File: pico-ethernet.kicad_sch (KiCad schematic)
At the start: 28 parts, among them J1 Conn_01x20_Pin, J2 Conn_01x02_Pin, J3 VR05S05, J4 SI-52003-F, J5 Conn_01x02, U1 ENC28J60x-SS, Y1 25MHz

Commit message: interrupt
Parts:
- J2: footprint Connector_PinSocket_2.54mm:PinSocket_1x04_P2.54mm_Vertical -> Connector_PinSocket_2.54mm:PinSocket_1x05_P2.54mm_Vertical; symbol Connector:Conn_01x04_Pin -> Connector:Conn_01x05_Pin
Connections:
- net at U1.4 (~{INT}): now also J2.5 (Pin_5)
- no-connect marks 17 -> 16
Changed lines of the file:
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@@
 	)
 	(no_connect
-		(at 105.41 83.82)
-	)
-	(no_connect
 		(at 82.55 48.26)
 	)
@@
 	(wire
 		(pts
-			(xy 46.99 57.15) (xy 46.99 54.61)
+			(xy 46.99 52.07) (xy 46.99 57.15)
+		)
+		(stroke
+			(width 0)
+			(type default)
+		)
+	)
+	(wire
+		(pts
+			(xy 72.39 64.77) (xy 36.83 64.77)
 		)
 		(stroke
@@
 	(wire
 		(pts
-			(xy 36.83 59.69) (xy 40.64 59.69)
+			(xy 52.07 54.61) (xy 52.07 62.23)
 		)
 		(stroke
@@
 	(wire
 		(pts
-			(xy 52.07 54.61) (xy 52.07 62.23)
+			(xy 166.37 77.47) (xy 166.37 80.01)
 		)
 		(stroke
@@
 	(wire
 		(pts
-			(xy 166.37 77.47) (xy 166.37 80.01)
+			(xy 151.13 101.6) (xy 152.4 101.6)
 		)
 		(stroke
@@
 	(wire
 		(pts
-			(xy 151.13 101.6) (xy 152.4 101.6)
+			(xy 82.55 81.28) (xy 97.79 81.28)
 		)
 		(stroke
@@
 	(wire
 		(pts
-			(xy 82.55 81.28) (xy 97.79 81.28)
+			(xy 46.99 52.07) (xy 36.83 52.07)
 		)
 		(stroke
@@
 	(wire
 		(pts
-			(xy 125.73 52.07) (xy 113.03 52.07)
+			(xy 40.64 57.15) (xy 36.83 57.15)
 		)
 		(stroke
@@
 	(wire
 		(pts
-			(xy 176.53 99.06) (xy 160.02 99.06)
+			(xy 125.73 52.07) (xy 113.03 52.07)
 		)
 		(stroke
@@
 	(wire
 		(pts
-			(xy 100.33 99.06) (xy 100.33 100.33)
+			(xy 176.53 99.06) (xy 160.02 99.06)
 		)
 		(stroke
@@
 	(wire
 		(pts
-			(xy 166.37 80.01) (xy 166.37 82.55)
+			(xy 100.33 99.06) (xy 100.33 100.33)
 		)
 		(stroke
@@
 	(wire
 		(pts
-			(xy 229.87 97.79) (xy 229.87 102.87)
+			(xy 166.37 80.01) (xy 166.37 82.55)
 		)
 		(stroke
@@
 	(wire
 		(pts
-			(xy 36.83 54.61) (xy 46.99 54.61)
+			(xy 229.87 97.79) (xy 229.87 102.87)
 		)
 		(stroke
@@
 	(wire
 		(pts
+			(xy 105.41 82.55) (xy 72.39 82.55)
+		)
+		(stroke
+			(width 0)
+			(type default)
+		)
+	)
+	(wire
+		(pts
 			(xy 105.41 73.66) (xy 97.79 73.66)
 		)
@@
 	(wire
 		(pts
-			(xy 36.83 52.07) (xy 43.18 52.07)
-		)
-		(stroke
-			(width 0)
-			(type default)
-		)
-	)
-	(wire
-		(pts
 			(xy 132.08 54.61) (xy 142.24 54.61)
 		)
@@
 	(wire
 		(pts
-			(xy 40.64 62.23) (xy 40.64 59.69)
+			(xy 40.64 57.15) (xy 40.64 62.23)
 		)
 		(stroke
@@
 	(wire
 		(pts
-			(xy 43.18 52.07) (xy 43.18 59.69)
+			(xy 43.18 49.53) (xy 43.18 59.69)
 		)
 		(stroke
@@
 	(wire
 		(pts
+			(xy 72.39 82.55) (xy 72.39 64.77)
+		)
+		(stroke
+			(width 0)
+			(type default)
+		)
+	)
+	(wire
+		(pts
 			(xy 120.65 153.67) (xy 120.65 143.51)
 		)
@@
 	(wire
 		(pts
+			(xy 43.18 49.53) (xy 36.83 49.53)
+		)
+		(stroke
+			(width 0)
+			(type default)
+		)
+	)
+	(wire
+		(pts
 			(xy 209.55 95.25) (xy 232.41 95.25)
 		)
@@
 	(wire
 		(pts
+			(xy 36.83 64.77) (xy 36.83 59.69)
+		)
+		(stroke
+			(width 0)
+			(type default)
+		)
+	)
+	(wire
+		(pts
 			(xy 82.55 78.74) (xy 105.41 78.74)
 		)
@@
 	(wire
 		(pts
+			(xy 105.41 83.82) (xy 105.41 82.55)
+		)
+		(stroke
+			(width 0)
+			(type default)
+		)
+	)
+	(wire
+		(pts
 			(xy 73.66 100.33) (xy 78.74 100.33)
 		)
@@
 			)
 		)
-		(property "Datasheet" ""
+		(property "Datasheet" "https://www.belfuse.com/resources/drawings/magneticsolutions/dr-mag-si-52003-f.pdf"
 			(at 245.11 87.63 0)
 			(effects
@@
 		(lib_name "GND_1")
 		(lib_id "power:GND")
-		(at 36.83 57.15 90)
+		(at 36.83 54.61 90)
 		(unit 1)
 		(exclude_from_sim no)
@@
 		(dnp no)
 		(property "Reference" "#PWR021"
-			(at 43.18 57.15 0)
+			(at 43.18 54.61 0)
 			(effects
 				(font
@@
 		)
 		(property "Value" "GND"
-			(at 40.132 57.15 90)
+			(at 40.132 54.61 90)
 			(effects
 				(font
@@
 		)
 		(property "Footprint" ""
-			(at 36.83 57.15 0)
+			(at 36.83 54.61 0)
 			(effects
 				(font
@@
 		)
 		(property "Datasheet" ""
-			(at 36.83 57.15 0)
+			(at 36.83 54.61 0)
 			(effects
 				(font
@@
 		)
 		(property "Description" "Power symbol creates a global label with name \"GND\" , ground"
-			(at 36.83 57.15 0)
+			(at 36.83 54.61 0)
 			(effects
 				(font
@@
 			)
 		)
-		(property "Datasheet" "VR05S05"
+		(property "Datasheet" "https://www.xppower.com/portals/0/pdfs/SF_VR05.pdf"
 			(at 102.87 156.21 0)
 			(effects
@@
 	)
 	(symbol
-		(lib_id "Connector:Conn_01x04_Pin")
+		(lib_id "Connector:Conn_01x05_Pin")
 		(at 31.75 54.61 0)
 		(unit 1)
@@
 		(fields_autoplaced yes)
 		(property "Reference" "J2"
-			(at 32.385 46.99 0)
+			(at 32.385 44.45 0)
 			(effects
 				(font
@@
 		)
 		(property "Value" "Conn_01x02_Pin"
-			(at 32.385 49.53 0)
+			(at 32.385 46.99 0)
 			(effects
 				(font
@@
 			)
 		)
-		(property "Footprint" "Connector_PinSocket_2.54mm:PinSocket_1x04_P2.54mm_Vertical"
+		(property "Footprint" "Connector_PinSocket_2.54mm:PinSocket_1x05_P2.54mm_Vertical"
 			(at 31.75 54.61 0)
 			(effects
@@
 			)
 		)
-		(property "Description" "Generic connector, single row, 01x04, script generated"
+		(property "Description" "Generic connector, single row, 01x05, script generated"
 			(at 31.75 54.61 0)
 			(effects
@@
 		(pin "4"
 		)
+		(pin "5"
+		)
 		(instances
 			(project "pico-ethernet"
@@
 			)
 		)
-		(property "Datasheet" "http://ww1.microchip.com/downloads/en/devicedoc/39662e.pdf"
+		(property "Datasheet" "https://ww1.microchip.com/downloads/en/DeviceDoc/39662e.pdf"
 			(at 123.19 86.36 0)
 			(effects
@@
 			)
 		)
-		(property "Datasheet" "~"
+		(property "Datasheet" "https://media.digikey.com/pdf/Data%20Sheets/CTS%20Corporation%20PDFs/445_Series.pdf"
 			(at 92.71 96.52 0)
 			(effects

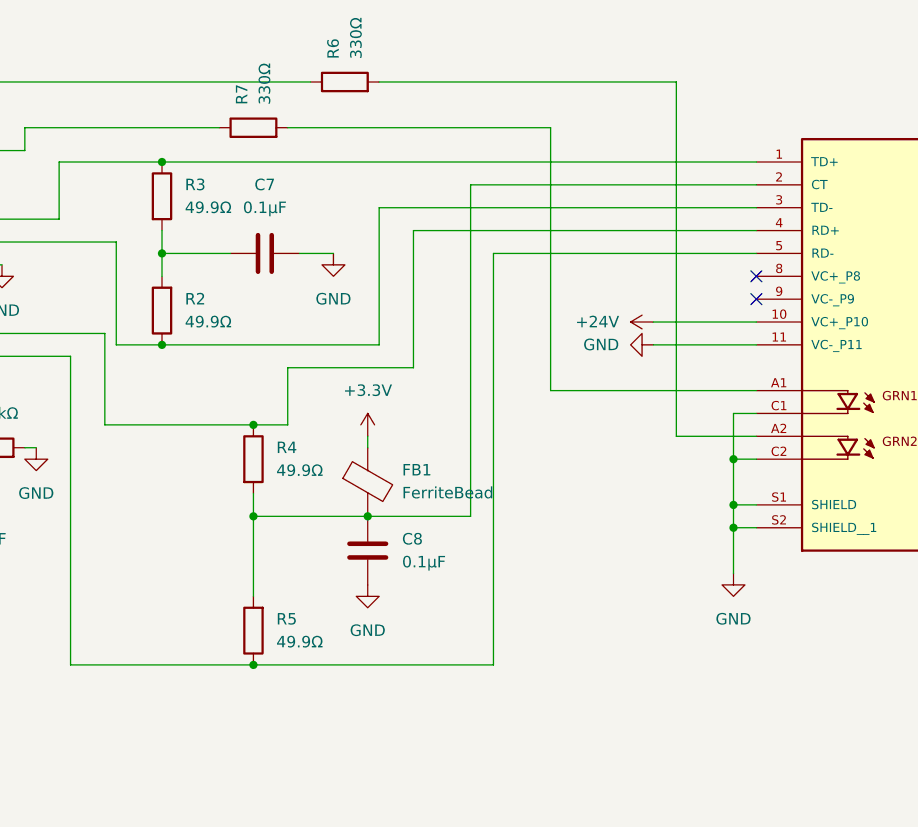
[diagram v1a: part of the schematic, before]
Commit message: TX RX swap
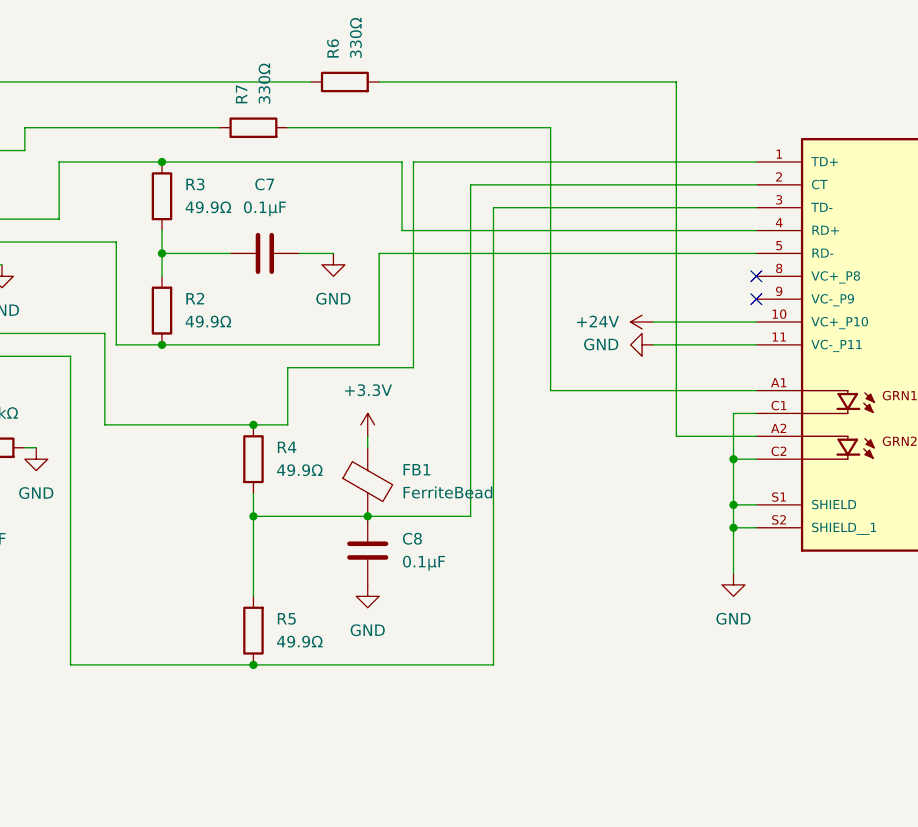
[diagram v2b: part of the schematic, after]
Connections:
- net at R3.1, U1.13 (TPIN+): now also J4.4 (RD+); no longer J4.1 (TD+)
- net at R2.1, U1.12 (TPIN-): now also J4.5 (RD-); no longer J4.3 (TD-)
- net at R4.1, U1.17 (TPOUT+): now also J4.1 (TD+); no longer J4.4 (RD+)
- net at R5.1, U1.16 (TPOUT-): now also J4.3 (TD-); no longer J4.5 (RD-)
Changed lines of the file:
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@@
+	)
+	(junction
+		(at 229.87 102.87)
+		(diameter 0)
+		(color 0 0 0 0)
+	)
+	(junction
+		(at 125.73 52.07)
+		(diameter 0)
+		(color 0 0 0 0)
+	)
+	(junction
+		(at 144.78 52.07)
+		(diameter 0)
+		(color 0 0 0 0)
+	)
+	(junction
+		(at 176.53 125.73)
+		(diameter 0)
+		(color 0 0 0 0)
+	)
+	(junction
+		(at 176.53 109.22)
+		(diameter 0)
+		(color 0 0 0 0)
+	)
+	(junction
+		(at 176.53 99.06)
+		(diameter 0)
+		(color 0 0 0 0)
+	)
+	(junction
+		(at 166.37 80.01)
+		(diameter 0)
+		(color 0 0 0 0)
+	)
+	(junction
+		(at 125.73 44.45)
+		(diameter 0)
+		(color 0 0 0 0)
+	)
+	(junction
+		(at 101.6 114.3)
+		(diameter 0)
+		(color 0 0 0 0)
+	)
+	(junction
+		(at 73.66 92.71)
+		(diameter 0)
+		(color 0 0 0 0)
+	)
+	(junction
+		(at 132.08 52.07)
+		(diameter 0)
+		(color 0 0 0 0)
+	)
+	(junction
+		(at 229.87 110.49)
+		(diameter 0)
+		(color 0 0 0 0)
+	)
+	(junction
+		(at 189.23 109.22)
+		(diameter 0)
+		(color 0 0 0 0)
+	)
+	(junction
+		(at 120.65 114.3)
+		(diameter 0)
+		(color 0 0 0 0)
+	)
+	(junction
+		(at 102.87 151.13)
+		(diameter 0)
+		(color 0 0 0 0)
+	)
+	(junction
+		(at 125.73 156.21)
+		(diameter 0)
+		(color 0 0 0 0)
 	)
 	(junction
@@
 	)
 	(junction
-		(at 229.87 102.87)
-		(diameter 0)
-		(color 0 0 0 0)
-	)
-	(junction
-		(at 125.73 52.07)
-		(diameter 0)
-		(color 0 0 0 0)
-	)
-	(junction
-		(at 144.78 52.07)
-		(diameter 0)
-		(color 0 0 0 0)
-	)
-	(junction
-		(at 176.53 125.73)
-		(diameter 0)
-		(color 0 0 0 0)
-	)
-	(junction
-		(at 176.53 109.22)
-		(diameter 0)
-		(color 0 0 0 0)
-	)
-	(junction
-		(at 176.53 99.06)
-		(diameter 0)
-		(color 0 0 0 0)
-	)
-	(junction
-		(at 166.37 80.01)
-		(diameter 0)
-		(color 0 0 0 0)
-	)
-	(junction
-		(at 125.73 44.45)
-		(diameter 0)
-		(color 0 0 0 0)
-	)
-	(junction
-		(at 101.6 114.3)
-		(diameter 0)
-		(color 0 0 0 0)
-	)
-	(junction
-		(at 73.66 92.71)
-		(diameter 0)
-		(color 0 0 0 0)
-	)
-	(junction
-		(at 132.08 52.07)
-		(diameter 0)
-		(color 0 0 0 0)
-	)
-	(junction
-		(at 229.87 110.49)
-		(diameter 0)
-		(color 0 0 0 0)
-	)
-	(junction
-		(at 189.23 109.22)
-		(diameter 0)
-		(color 0 0 0 0)
-	)
-	(junction
-		(at 120.65 114.3)
-		(diameter 0)
-		(color 0 0 0 0)
-	)
-	(junction
-		(at 102.87 151.13)
-		(diameter 0)
-		(color 0 0 0 0)
-	)
-	(junction
-		(at 125.73 156.21)
-		(diameter 0)
-		(color 0 0 0 0)
-	)
-	(junction
 		(at 132.08 44.45)
 		(diameter 0)
@@
 	(wire
 		(pts
+			(xy 203.2 74.93) (xy 232.41 74.93)
+		)
+		(stroke
+			(width 0)
+			(type default)
+		)
+	)
+	(wire
+		(pts
 			(xy 46.99 52.07) (xy 46.99 57.15)
 		)
@@
 	(wire
 		(pts
+			(xy 194.31 69.85) (xy 232.41 69.85)
+		)
+		(stroke
+			(width 0)
+			(type default)
+		)
+	)
+	(wire
+		(pts
+			(xy 203.2 74.93) (xy 203.2 125.73)
+		)
+		(stroke
+			(width 0)
+			(type default)
+		)
+	)
+	(wire
+		(pts
 			(xy 140.97 93.98) (xy 144.78 93.98)
 		)
@@
 	(wire
 		(pts
-			(xy 203.2 80.01) (xy 203.2 125.73)
-		)
-		(stroke
-			(width 0)
-			(type default)
-		)
-	)
-	(wire
-		(pts
 			(xy 52.07 54.61) (xy 52.07 62.23)
 		)
@@
 	(wire
 		(pts
-			(xy 194.31 77.47) (xy 194.31 92.71)
+			(xy 194.31 69.85) (xy 194.31 92.71)
 		)
 		(stroke
@@
 	(wire
 		(pts
-			(xy 232.41 74.93) (xy 190.5 74.93)
-		)
-		(stroke
-			(width 0)
-			(type default)
-		)
-	)
-	(wire
-		(pts
 			(xy 166.37 80.01) (xy 173.99 80.01)
 		)
@@
 	(wire
 		(pts
-			(xy 232.41 80.01) (xy 203.2 80.01)
-		)
-		(stroke
-			(width 0)
-			(type default)
-		)
-	)
-	(wire
-		(pts
 			(xy 132.08 52.07) (xy 144.78 52.07)
 		)
@@
 	(wire
 		(pts
+			(xy 190.5 80.01) (xy 232.41 80.01)
+		)
+		(stroke
+			(width 0)
+			(type default)
+		)
+	)
+	(wire
+		(pts
 			(xy 180.34 66.04) (xy 209.55 66.04)
 		)
@@
 	(wire
 		(pts
+			(xy 193.04 69.85) (xy 193.04 77.47)
+		)
+		(stroke
+			(width 0)
+			(type default)
+		)
+	)
+	(wire
+		(pts
 			(xy 232.41 107.95) (xy 229.87 107.95)
 		)
@@
 	(wire
 		(pts
-			(xy 166.37 69.85) (xy 232.41 69.85)
+			(xy 190.5 80.01) (xy 190.5 90.17)
 		)
 		(stroke
@@
 	(wire
 		(pts
-			(xy 232.41 77.47) (xy 194.31 77.47)
-		)
-		(stroke
-			(width 0)
-			(type default)
-		)
-	)
-	(wire
-		(pts
 			(xy 86.36 35.56) (xy 82.55 35.56)
 		)
@@
 	(wire
 		(pts
-			(xy 190.5 74.93) (xy 190.5 90.17)
-		)
-		(stroke
-			(width 0)
-			(type default)
-		)
-	)
-	(wire
-		(pts
 			(xy 189.23 109.22) (xy 200.66 109.22)
 		)
@@
 	(wire
 		(pts
+			(xy 166.37 69.85) (xy 193.04 69.85)
+		)
+		(stroke
+			(width 0)
+			(type default)
+		)
+	)
+	(wire
+		(pts
 			(xy 54.61 54.61) (xy 52.07 54.61)
 		)
@@
 		)
 		(stroke
+			(width 0)
+			(type default)
+		)
+	)
+	(wire
+		(pts
+			(xy 193.04 77.47) (xy 232.41 77.47)
+		)
+		(stroke

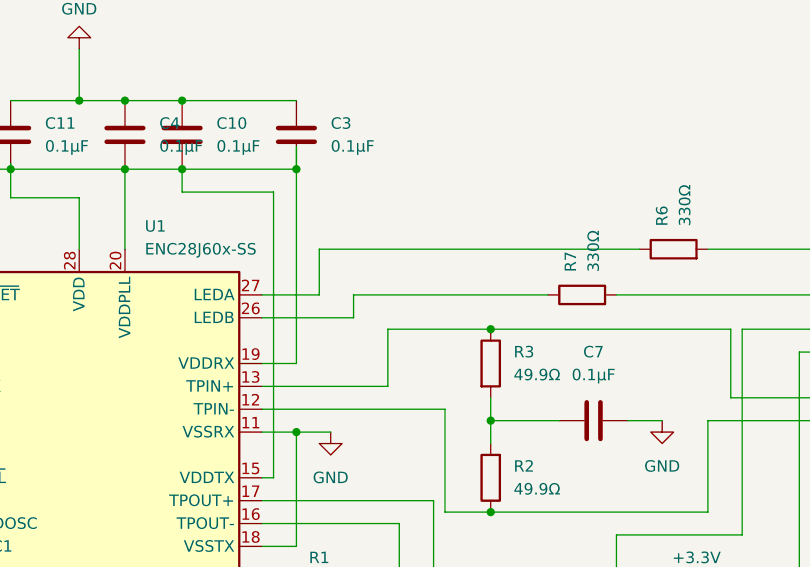
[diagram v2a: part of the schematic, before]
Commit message: 3v reroute
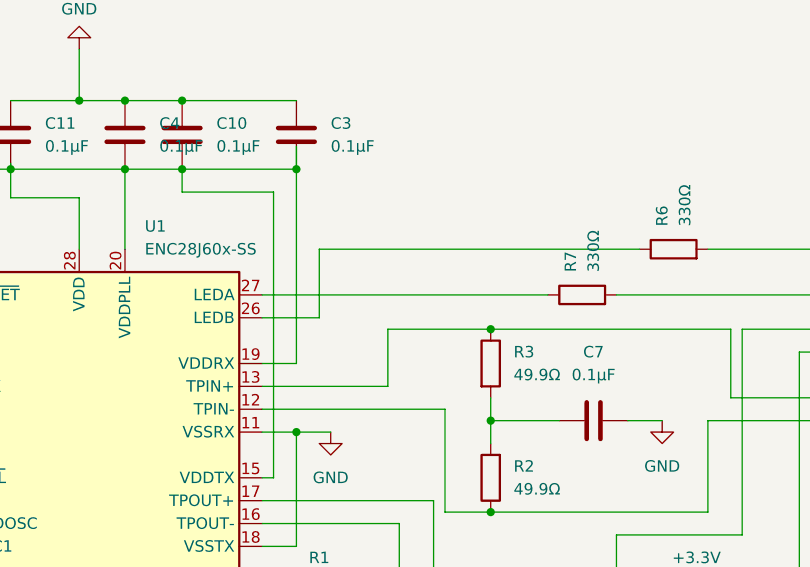
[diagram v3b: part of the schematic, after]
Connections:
- net at R6.1: now also U1.26 (LEDB); no longer U1.27 (LEDA)
- net at R7.1: now also U1.27 (LEDA); no longer U1.26 (LEDB)
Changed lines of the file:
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@@
-	(wire
-		(pts
-			(xy 151.13 68.58) (xy 140.97 68.58)
-		)
-		(stroke
-			(width 0)
-			(type default)
-		)
-	)
 	(wire
 		(pts
@@
 	(wire
 		(pts
-			(xy 140.97 66.04) (xy 147.32 66.04)
-		)
-		(stroke
-			(width 0)
-			(type default)
-		)
-	)
-	(wire
-		(pts
 			(xy 132.08 44.45) (xy 144.78 44.45)
 		)
@@
 	(wire
 		(pts
+			(xy 147.32 68.58) (xy 140.97 68.58)
+		)
+		(stroke
+			(width 0)
+			(type default)
+		)
+	)
+	(wire
+		(pts
 			(xy 181.61 80.01) (xy 185.42 80.01)
 		)
@@
 	(wire
 		(pts
-			(xy 172.72 66.04) (xy 151.13 66.04)
+			(xy 140.97 66.04) (xy 172.72 66.04)
 		)
 		(stroke
@@
 	(wire
 		(pts
-			(xy 147.32 60.96) (xy 147.32 66.04)
-		)
-		(stroke
-			(width 0)
-			(type default)
-		)
-	)
-	(wire
-		(pts
 			(xy 176.53 125.73) (xy 203.2 125.73)
 		)
@@
 	(wire
 		(pts
-			(xy 151.13 66.04) (xy 151.13 68.58)
-		)
-		(stroke
-			(width 0)
-			(type default)
-		)
-	)
-	(wire
-		(pts
 			(xy 144.78 81.28) (xy 148.59 81.28)
 		)
@@
 		)
 		(stroke
+			(width 0)
+			(type default)
+		)
+	)
+	(wire
+		(pts
+			(xy 147.32 60.96) (xy 147.32 68.58)
+		)
+		(stroke

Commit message: vanity
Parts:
- R6, R7: value 330Ω -> 180Ω
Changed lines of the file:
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@@
 	(wire
 		(pts
-			(xy 203.2 74.93) (xy 232.41 74.93)
+			(xy 205.74 74.93) (xy 232.41 74.93)
 		)
 		(stroke
@@
 	(wire
 		(pts
-			(xy 194.31 69.85) (xy 232.41 69.85)
+			(xy 196.85 69.85) (xy 232.41 69.85)
 		)
 		(stroke
@@
 	(wire
 		(pts
-			(xy 203.2 74.93) (xy 203.2 125.73)
+			(xy 205.74 74.93) (xy 205.74 125.73)
 		)
 		(stroke
@@
 	(wire
 		(pts
-			(xy 194.31 92.71) (xy 180.34 92.71)
+			(xy 196.85 92.71) (xy 180.34 92.71)
 		)
 		(stroke
@@
 	(wire
 		(pts
-			(xy 194.31 69.85) (xy 194.31 92.71)
+			(xy 196.85 69.85) (xy 196.85 92.71)
 		)
 		(stroke
@@
 	(wire
 		(pts
-			(xy 176.53 125.73) (xy 203.2 125.73)
+			(xy 176.53 125.73) (xy 205.74 125.73)
 		)
 		(stroke
@@
 	(wire
 		(pts
-			(xy 193.04 69.85) (xy 193.04 77.47)
+			(xy 190.5 69.85) (xy 190.5 77.47)
 		)
 		(stroke
@@
 	(wire
 		(pts
-			(xy 166.37 69.85) (xy 193.04 69.85)
+			(xy 166.37 69.85) (xy 190.5 69.85)
 		)
 		(stroke
@@
 	(wire
 		(pts
-			(xy 193.04 77.47) (xy 232.41 77.47)
+			(xy 190.5 77.47) (xy 232.41 77.47)
 		)
 		(stroke
@@
 			)
 		)
-		(property "Value" "330Ω"
+		(property "Value" "180Ω"
 			(at 187.96 58.42 0)
 			(effects
@@
 			)
 		)
-		(property "Value" "330Ω"
+		(property "Value" "180Ω"
 			(at 177.8 63.5 0)
 			(effects

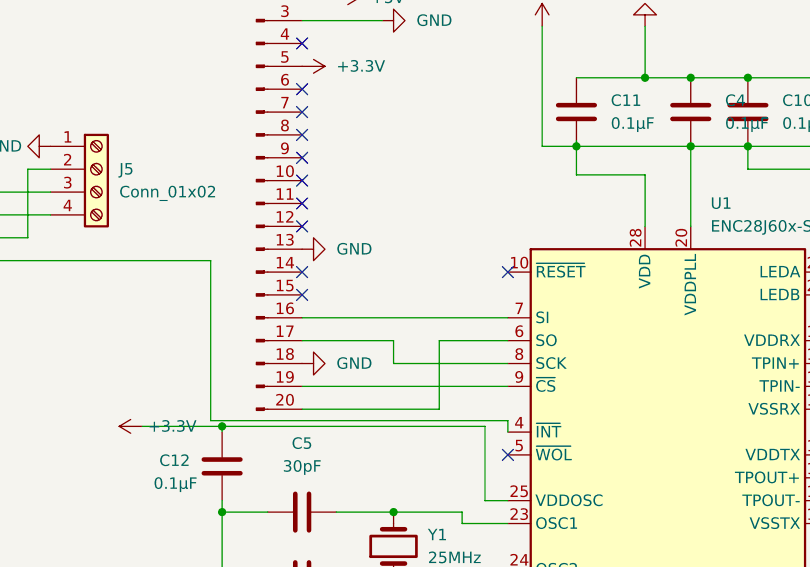
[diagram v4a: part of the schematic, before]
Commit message: connect reset
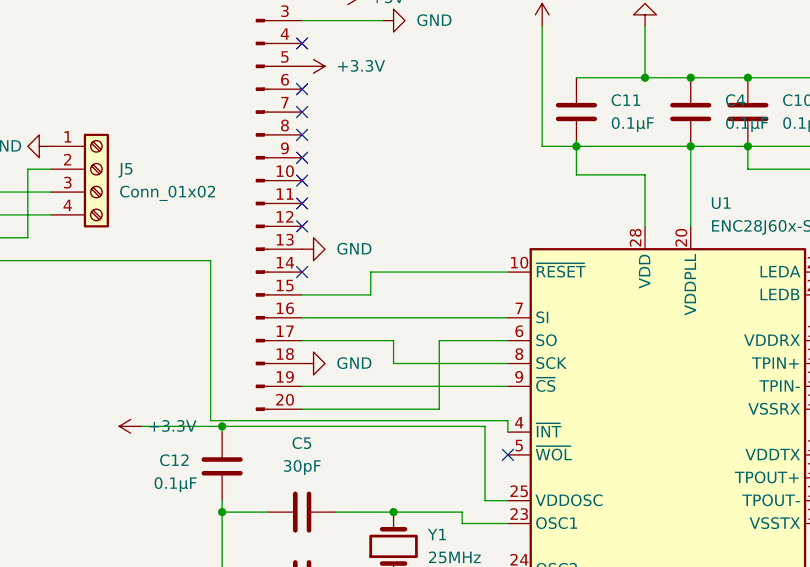
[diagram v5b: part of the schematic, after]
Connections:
- net at J1.15 (Pin_15): now also U1.10 (~{RESET})
- no-connect marks 16 -> 14
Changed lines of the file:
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@@
-	)
-	(no_connect
-		(at 105.41 66.04)
-	)
-	(no_connect
-		(at 82.55 68.58)
 	)
 	(no_connect
@@
 	(wire
 		(pts
+			(xy 90.17 68.58) (xy 82.55 68.58)
+		)
+		(stroke
+			(width 0)
+			(type default)
+		)
+	)
+	(wire
+		(pts
 			(xy 113.03 52.07) (xy 109.22 52.07)
 		)
@@
 	(wire
 		(pts
+			(xy 90.17 66.04) (xy 90.17 68.58)
+		)
+		(stroke
+			(width 0)
+			(type default)
+		)
+	)
+	(wire
+		(pts
 			(xy 113.03 44.45) (xy 120.65 44.45)
 		)
@@
 		)
 		(stroke
+			(width 0)
+			(type default)
+		)
+	)
+	(wire
+		(pts
+			(xy 105.41 66.04) (xy 90.17 66.04)
+		)
+		(stroke
